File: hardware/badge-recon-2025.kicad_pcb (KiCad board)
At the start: 2 copper layers, 78.1 x 100 mm, 84 parts, among them J1 EXPANSION, J3 Battery, J5 OLED, P1 USB_C_Plug_USB2.0, Q1 DMG3415U-7, SW1 SW_Push, SW2 SW_Push, SW3 ON, SW4 SOURCE MAG, SW5 SW_Push, SW6 SW_Push, SW7 RESET, SW8 BOOT, U1 PN7150B0HN_C11002E-PN7150B0HN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, U2 RP2040, U3 AP2114H, U4 W25Q16JV, U5 TC4424, Y1 27.12Mhz, Y2 ABM8-272-T3

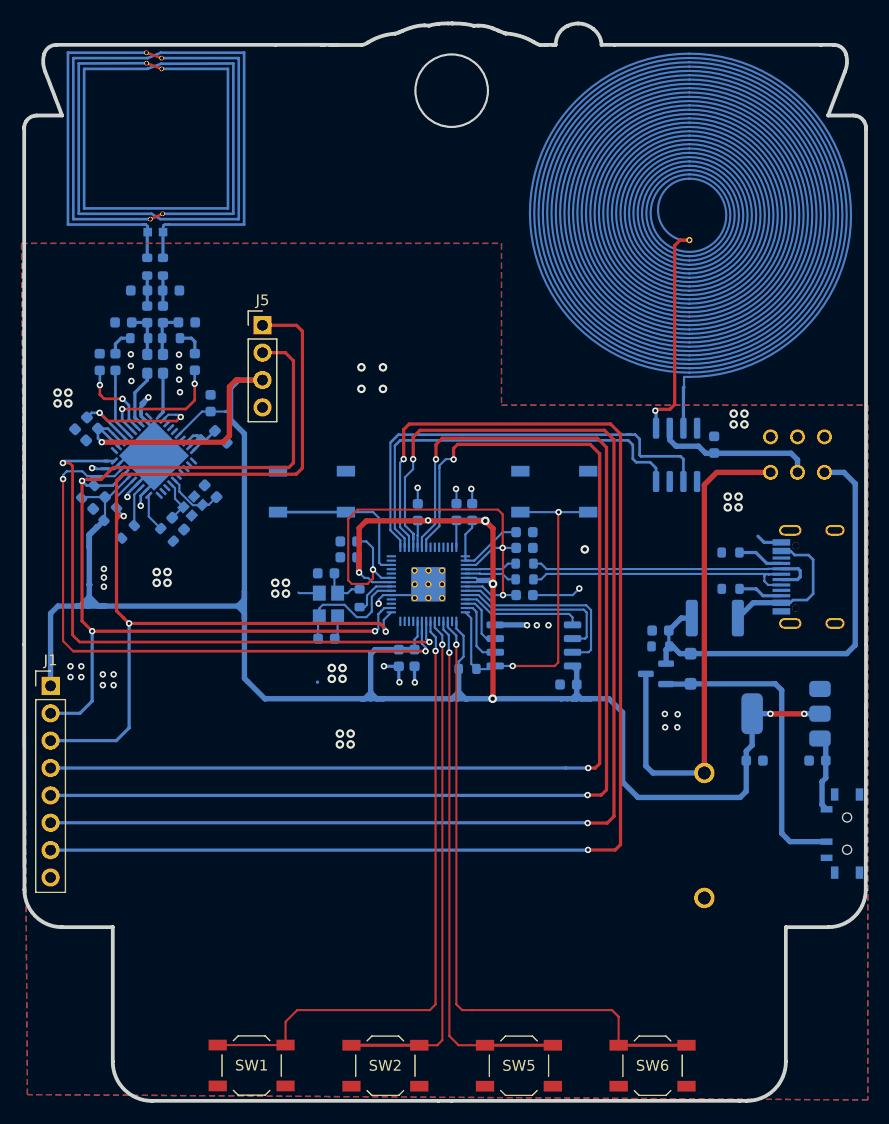
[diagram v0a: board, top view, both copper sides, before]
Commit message: fix(Hw): set component as dnp & move routes
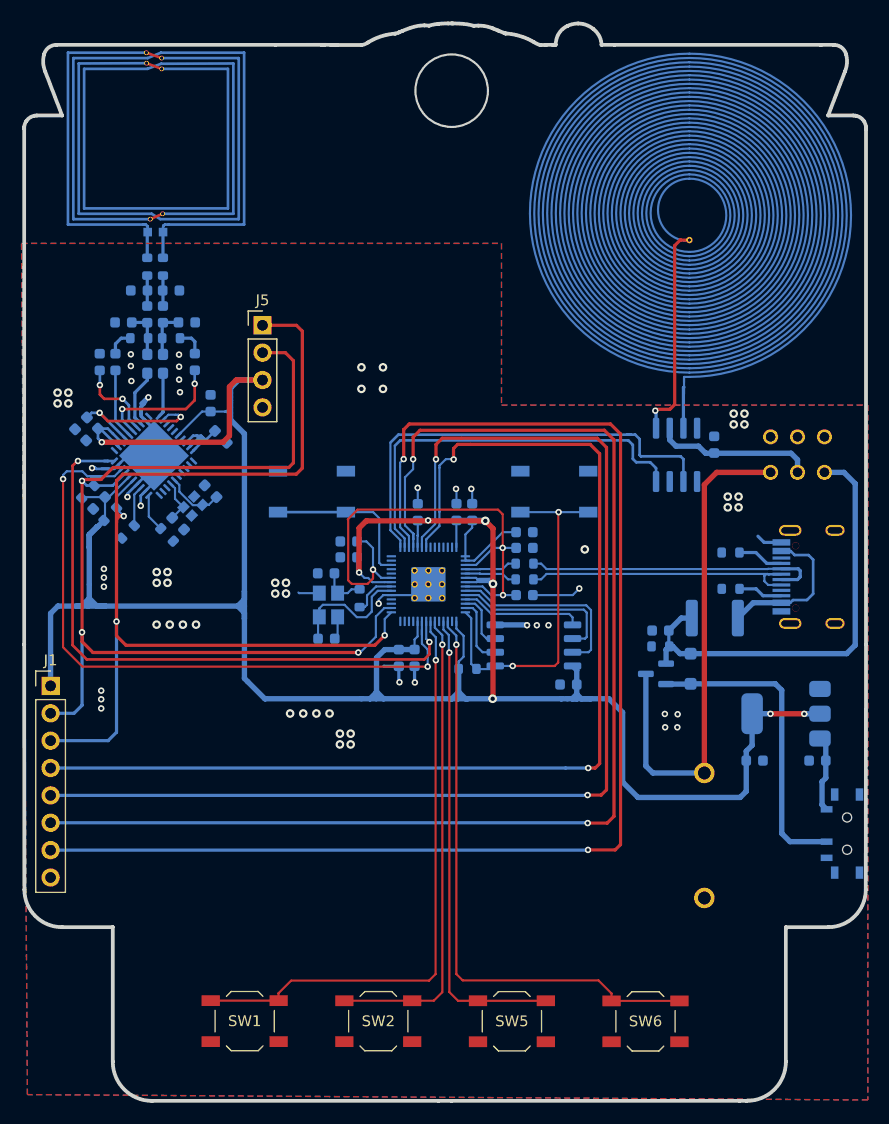
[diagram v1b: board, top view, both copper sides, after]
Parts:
- moved SW2 4.18 mm to (146.6, 137.7)
- moved SW5 4.18 mm to (159.0, 137.7)
- moved SW6 4.17 mm to (171.4, 137.7)
- moved SW1 4.17 mm to (134.2, 137.7)
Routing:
- net /BUTTON_4: track 60.4 -> 55.2 mm
- net /BUTTON_3: track 48.7 -> 43.9 mm
- net /BUTTON_2: track 47.8 -> 44.1 mm
- net /BUTTON_1: track 58.8 -> 55.3 mm
- net /IRQ: track 61.3 -> 63.9 mm
- net /SCL: track 92.3 -> 94.6 mm
- net +3V3: track 272.9 -> 271.2 mm
- net /SDA: track 99.4 -> 100.9 mm
- net /VEN: track 57.4 -> 58.2 mm
- net GND: vias 70 -> 68

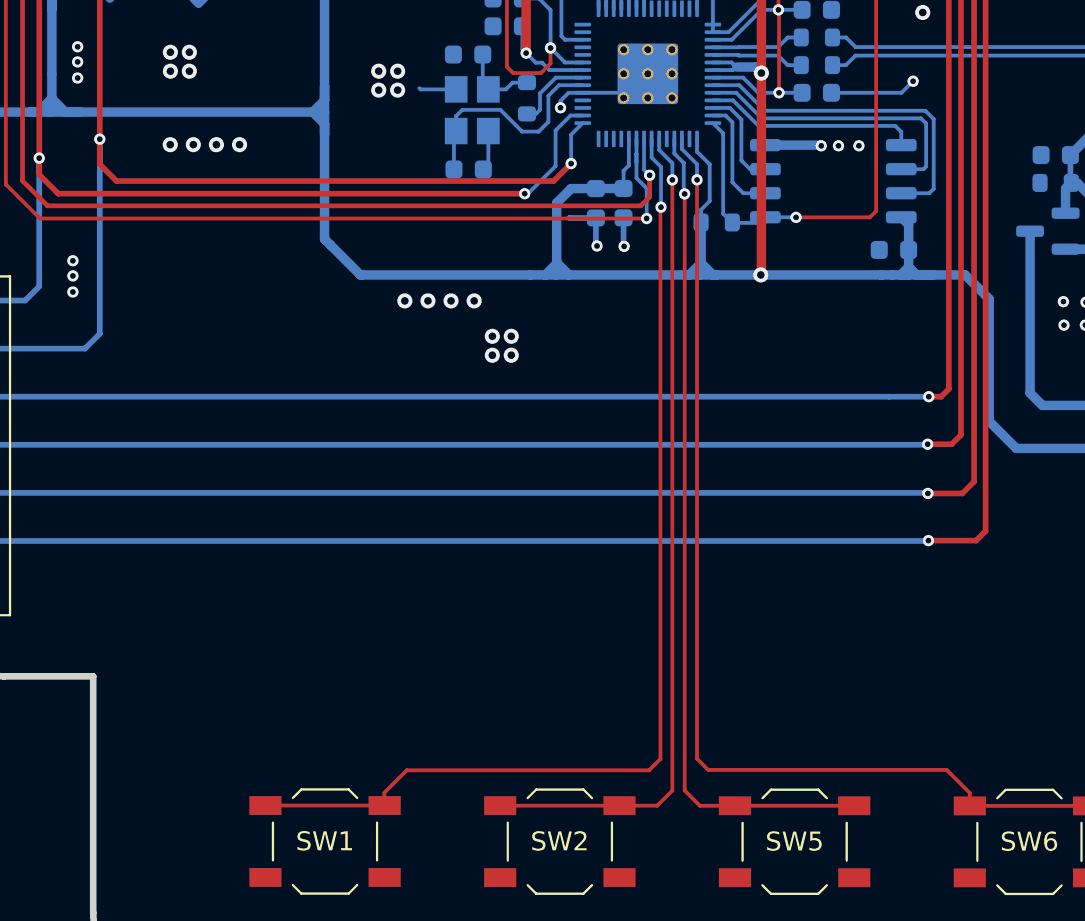
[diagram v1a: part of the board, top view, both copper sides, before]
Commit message: fix(Hw): fix traces
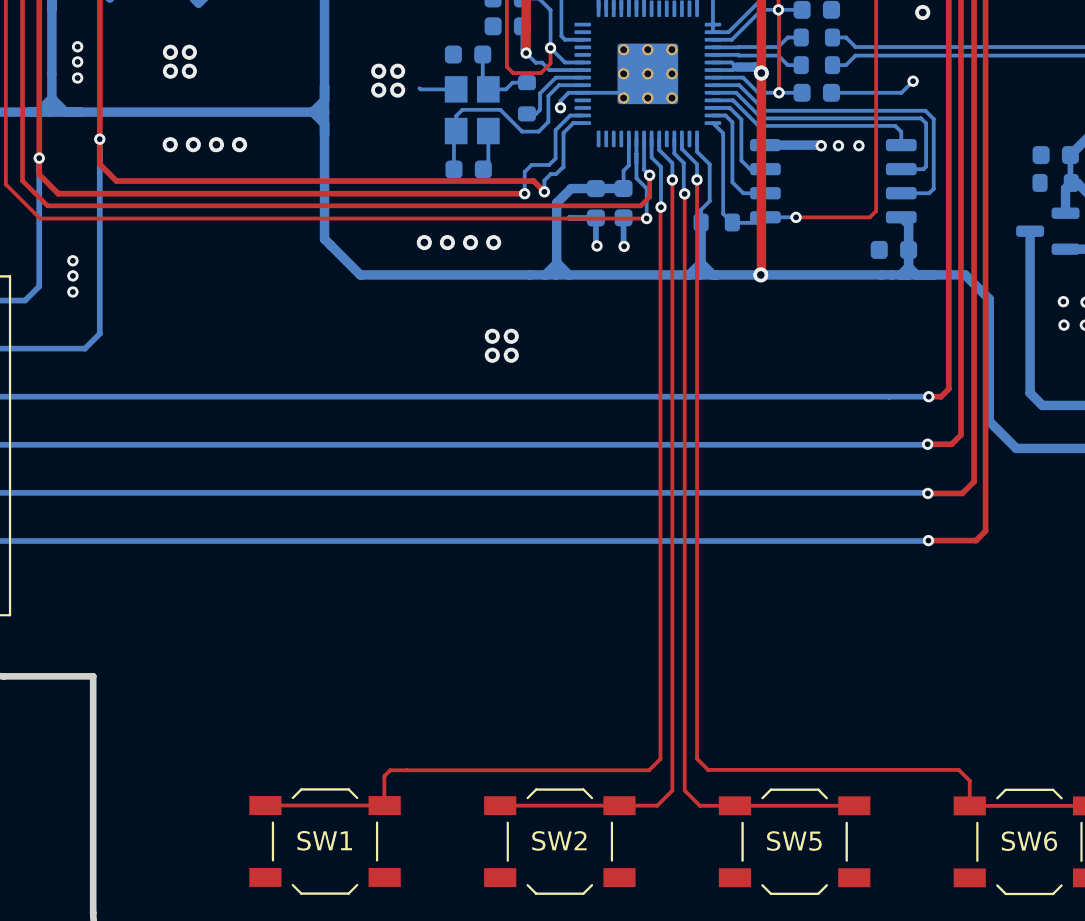
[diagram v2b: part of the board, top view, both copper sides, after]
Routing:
- net /SDA: track 100.9 -> 101.9 mm
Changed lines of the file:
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@@
 	)
 	(via
-		(at 140.82 109.13)
+		(at 141.85 106.05)
 		(size 0.8)
 		(drill 0.4)
@@
 	)
 	(via
-		(at 142.04 109.13)
+		(at 143.07 106.05)
 		(size 0.8)
 		(drill 0.4)
@@
 	)
 	(via
-		(at 138.38 109.13)
+		(at 139.41 106.05)
 		(size 0.8)
 		(drill 0.4)
@@
 	)
 	(via
-		(at 139.6 109.13)
+		(at 140.63 106.05)
 		(size 0.8)
 		(drill 0.4)
@@
 	)
 	(segment
-		(start 146.240477 102.8)
+		(start 145.16 102.8)
 		(end 123.15 102.8)
 		(width 0.3)
@@
 	)
 	(segment
+		(start 145.16 102.8)
+		(end 145.18 102.8)
+		(width 0.3)
+		(layer "F.Cu")
+		(net 27)
+	)
+	(segment
 		(start 138.95 86.92)
 		(end 139.52 86.35)
@@
 	)
 	(segment
-		(start 147.161837 101.87864)
-		(end 146.240477 102.8)
+		(start 145.18 102.8)
+		(end 145.75 103.37)
 		(width 0.3)
 		(layer "F.Cu")
@@
 	)
 	(via
-		(at 147.161837 101.87864)
+		(at 145.75 103.37)
 		(size 0.6)
 		(drill 0.3)
@@
 	)
 	(segment
-		(start 147.161837 100.353163)
-		(end 147.775 99.74)
+		(start 146.37 102.43)
+		(end 146.72 102.08)
 		(width 0.2)
 		(layer "B.Cu")
@@
 	)
 	(segment
-		(start 121.49 111.65)
-		(end 116.15 111.65)
-		(width 0.3)
+		(start 145.75 102.77)
+		(end 146.09 102.43)
+		(width 0.2)
 		(layer "B.Cu")
 		(net 27)
 	)
 	(segment
-		(start 147.161837 101.87864)
-		(end 147.161837 100.353163)
-		(width 0.2)
+		(start 121.49 111.65)
+		(end 116.15 111.65)
+		(width 0.3)
 		(layer "B.Cu")
 		(net 27)
@@
 	)
 	(segment
+		(start 147.28 99.74)
+		(end 147.775 99.74)
+		(width 0.2)
+		(layer "B.Cu")
+		(net 27)
+	)
+	(segment
 		(start 123.847651 87.463902)
 		(end 122.271363 89.04019)
@@
 	)
 	(segment
+		(start 146.76 100.26)
+		(end 147.28 99.74)
+		(width 0.2)
+		(layer "B.Cu")
+		(net 27)
+	)
+	(segment
+		(start 146.76 102.08)
+		(end 146.76 100.26)
+		(width 0.2)
+		(layer "B.Cu")
+		(net 27)
+	)
+	(segment
+		(start 145.75 103.37)
+		(end 145.75 102.77)
+		(width 0.2)
+		(layer "B.Cu")
+		(net 27)
+	)
+	(segment
+		(start 146.72 102.08)
+		(end 146.76 102.08)
+		(width 0.2)
+		(layer "B.Cu")
+		(net 27)
+	)
+	(segment
 		(start 122.271363 89.04019)
 		(end 122.271363 90.046637)
@@
 	)
 	(segment
+		(start 146.09 102.43)
+		(end 146.37 102.43)
+		(width 0.2)
+		(layer "B.Cu")
+		(net 27)
+	)
+	(segment
 		(start 120.84 87.41)
 		(end 121.95 86.3)
@@
 	)
 	(segment
-		(start 119.507398 87.976637)
-		(end 119.07171 87.540949)
-		(width 0.25)
+		(start 146.34 100.114314)
+		(end 147.114314 99.34)
+		(width 0.2)
 		(layer "B.Cu")
 		(net 28)
 	)
 	(segment
-		(start 147.13 99.34)
-		(end 147.775 99.34)
-		(width 0.2)
+		(start 119.507398 87.976637)
+		(end 119.07171 87.540949)
+		(width 0.25)
 		(layer "B.Cu")
 		(net 28)
@@
 	)
 	(segment
-		(start 144.71 103.47)
-		(end 144.88 103.47)
+		(start 145.077843 101.952157)
+		(end 146.002157 101.952157)
 		(width 0.2)
 		(layer "B.Cu")
@@
 	)
 	(segment
-		(start 119.07171 108.36829)
-		(end 119.07171 101.59171)
-		(width 0.3)
+		(start 146.002157 101.952157)
+		(end 146.34 101.614314)
+		(width 0.2)
 		(layer "B.Cu")
 		(net 28)
 	)
 	(segment
-		(start 146.34 102.01)
-		(end 146.34 100.13)
+		(start 146.34 101.614314)
+		(end 146.34 100.114314)
 		(width 0.2)
 		(layer "B.Cu")
@@
 	)
 	(segment
+		(start 147.114314 99.34)
+		(end 147.775 99.34)
+		(width 0.2)
+		(layer "B.Cu")
+		(net 28)
+	)
+	(segment
+		(start 119.07171 108.36829)
+		(end 119.07171 101.59171)
+		(width 0.3)
+		(layer "B.Cu")
+		(net 28)
+	)
+	(segment
 		(start 120.201363 87.976637)
 		(end 119.507398 87.976637)
@@
 	)
 	(segment
-		(start 146.34 100.13)
-		(end 147.13 99.34)
+		(start 144.71 102.32)
+		(end 145.077843 101.952157)
 		(width 0.2)
 		(layer "B.Cu")
@@
 	)
 	(segment
-		(start 144.88 103.47)
-		(end 146.34 102.01)
+		(start 144.71 103.47)
+		(end 144.71 102.32)
 		(width 0.2)
 		(layer "B.Cu")
@@
 	)
 	(segment
+		(start 137.61 133.92)
+		(end 138.48 133.92)
+		(width 0.2)
+		(layer "F.Cu")
+		(net 40)
+	)
+	(segment
 		(start 151.88 133.32)
 		(end 151.28 133.92)
@@
 	)
 	(segment
-		(start 138.48 133.92)
-		(end 137.3 135.1)
+		(start 137.3 135.26)
+		(end 137.3 134.23)
 		(width 0.2)
 		(layer "F.Cu")
@@
 	)
 	(segment
-		(start 137.3 135.1)
-		(end 137.3 135.765326)
+		(start 137.3 134.23)
+		(end 137.61 133.92)
 		(width 0.2)
 		(layer "F.Cu")
@@
 	)
 	(segment
-		(start 154.4 133.9)
-		(end 153.81 133.31)
+		(start 168.214674 135.8)
+		(end 168.214674 134.474674)
 		(width 0.2)
 		(layer "F.Cu")
@@
 	)
 	(segment
-		(start 167 133.9)
-		(end 154.4 133.9)
+		(start 168.214674 134.474674)
+		(end 167.64 133.9)
 		(width 0.2)
 		(layer "F.Cu")
@@
 	)
 	(segment
-		(start 168.214674 135.8)
-		(end 168.214674 135.114674)
+		(start 167.64 133.9)
+		(end 154.4 133.9)
 		(width 0.2)
 		(layer "F.Cu")
@@
 	)
 	(segment
-		(start 168.214674 135.114674)
-		(end 167 133.9)
+		(start 154.4 133.9)
+		(end 153.81 133.31)
 		(width 0.2)
 		(layer "F.Cu")

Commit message: feat(Hw):Update_Labels
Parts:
- added G***: LOGO, Aesthetics:electronic_cats_logo_8x6, B.Cu at (147.8, 69.3)
- added kibuzzard-6814FFA5: G***, kibuzzard-6814FFA5, B.Cu at (185.8, 124.0)
- added kibuzzard-6814FFAA: G***, kibuzzard-6814FFAA, B.Cu at (185.8, 117.7)
- added kibuzzard-68150444: G***, kibuzzard-68150444, B.Cu at (140.4, 84.5)
- added kibuzzard-6815045B: G***, kibuzzard-6815045B, B.Cu at (162.9, 84.5)
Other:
- board text added: "Badge Recon v1.0"
- board text added: "MAGSPOOF"
- board text added: "NFC"
- board text added: "https://github.com /ElectronicCats /badge-recon-2025"
- board text removed: "- Check PN7150 crystal - Check RP2040 crystal"
